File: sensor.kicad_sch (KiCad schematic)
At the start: 36 parts, among them J10 Conn_01x01_Pin, J5 Conn_01x07_Pin, J8 Conn_01x08_Pin, U3 MIC5504-3.3YM5

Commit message: Cleanup
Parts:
- removed R16: 0k, Resistor_SMD:R_0402_1005Metric_Pad0.72x0.64mm_HandSolder, symbol Device:R_Small
- JP1: footprint Jumper:SolderJumper-3_P1.3mm_Open_RoundedPad1.0x1.5mm -> Jumper:SolderJumper-3_P1.3mm_Bridged2Bar12_RoundedPad1.0x1.5mm
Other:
- note added: "By default VCC is supplied by the 5V line on the VIK connector but we can connect the 3.3V VIK source to VCC using the solder jumper, or connect the controllers 5V supply via the VCC header by cutting the jumper trace and leaving the jumber unconnected."
- note removed: "By default VCC is supplied by the 5V line on the VIK connector via the 0k resistor. If removed we can try and be compatible with the Cirque. In this case we can either connect the 3.3V VIK source to VCC using the solder jumper, or connect the controllers 5V supply via the VCC header."
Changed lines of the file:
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@@
   (junction (at 104.14 43.18) (diameter 0) (color 0 0 0 0)
-  )
-  (junction (at 176.53 33.02) (diameter 0) (color 0 0 0 0)
   )
   (junction (at 186.69 33.02) (diameter 0) (color 0 0 0 0)
@@
     (stroke (width 0) (type default))
   )
-  (wire (pts (xy 176.53 25.4) (xy 176.53 26.67))
-    (stroke (width 0) (type default))
-  )
   (wire (pts (xy 99.06 60.96) (xy 99.06 59.69))
     (stroke (width 0) (type default))
@@
     (stroke (width 0) (type default))
   )
-  (wire (pts (xy 168.91 33.02) (xy 176.53 33.02))
+  (wire (pts (xy 168.91 33.02) (xy 179.07 33.02))
     (stroke (width 0) (type default))
   )
@@
     (stroke (width 0) (type default))
   )
-  (wire (pts (xy 176.53 31.75) (xy 176.53 33.02))
-    (stroke (width 0) (type default))
-  )
   (wire (pts (xy 175.26 86.36) (xy 177.8 86.36))
     (stroke (width 0) (type default))
@@
     (stroke (width 0) (type default))
   )
-  (wire (pts (xy 176.53 33.02) (xy 179.07 33.02))
-    (stroke (width 0) (type default))
-  )
   (wire (pts (xy 121.92 87.63) (xy 127 87.63))
     (stroke (width 0) (type default))
@@
     (effects (font (size 1.27 1.27)) (justify left bottom))
   )
-  (text "By default VCC is supplied by the 5V\nline on the VIK connector via the 0k\nresistor. If removed we can try and\nbe compatible with the Cirque. In\nthis case we can either connect the\n3.3V VIK source to VCC using the solder\njumper, or connect the controllers 5V\nsupply via the VCC header."
+  (text "By default VCC is supplied by the 5V\nline on the VIK connector but we can\nconnect the 3.3V VIK source to VCC using\nthe solder jumper, or connect the\ncontrollers 5V supply via the VCC header\nby cutting the jumper trace and leaving\nthe jumber unconnected."
     (at 148.59 60.96 0)
     (effects (font (size 1.27 1.27)) (justify left bottom))
@@
   (label "CHANGE" (at 196.85 125.73 0) (fields_autoplaced)
     (effects (font (size 1.27 1.27)) (justify left bottom))
-  )
-  (label "VIK_5V" (at 176.53 25.4 180) (fields_autoplaced)
-    (effects (font (size 1.27 1.27)) (justify right bottom))
   )
   (label "SCL" (at 72.39 119.38 180) (fields_autoplaced)
@@
       (effects (font (size 1.27 1.27)) hide)
     )
-    (property "Footprint" "Jumper:SolderJumper-3_P1.3mm_Open_RoundedPad1.0x1.5mm" (at 160.02 29.21 0)
+    (property "Footprint" "Jumper:SolderJumper-3_P1.3mm_Bridged2Bar12_RoundedPad1.0x1.5mm" (at 160.02 29.21 0)
       (effects (font (size 1.27 1.27)) hide)
     )
@@
         )
       )
-    )
-  )
-  (symbol (lib_id "Device:R_Small") (at 176.53 29.21 0) (unit 1)
-    (in_bom yes) (on_board yes) (dnp no) (fields_autoplaced)
-    (property "Reference" "R16" (at 179.07 27.94 0)
-      (effects (font (size 1.27 1.27)) (justify left))
-    )
-    (property "Value" "0k" (at 179.07 30.48 0)
-      (effects (font (size 1.27 1.27)) (justify left))
-    )
-    (property "Footprint" "Resistor_SMD:R_0402_1005Metric_Pad0.72x0.64mm_HandSolder" (at 176.53 29.21 0)
-      (effects (font (size 1.27 1.27)) hide)
-    )
-    (property "Datasheet" "~" (at 176.53 29.21 0)
-      (effects (font (size 1.27 1.27)) hide)
-    )
-    (property "LCSC" "C17168" (at 179.07 27.94 0)
-      (effects (font (size 1.27 1.27)) hide)
-    )
-    (pin "2")
-    (pin "1")
-    (instances
-      (project "trackpad"
-        (path "/3796446b-0052-4d89-b512-07a2e9135d0d/2780c9a8-e5e0-42e8-93d7-9eb6f8aa439b"
-          (reference "R16") (unit 1)
-        )
-      )

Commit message: Modifications before initial order.
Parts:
- C29: LCSC C52923 -> C1525
- R10: LCSC C25744 -> C25752
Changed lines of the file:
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@@
       (effects (font (size 1.27 1.27)) hide)
     )
-    (property "LCSC" "C25744" (at 176.53 36.83 0)
+    (property "LCSC" "C25752" (at 176.53 36.83 0)
       (effects (font (size 1.27 1.27)) hide)
     )
@@
       (effects (font (size 1.27 1.27)) hide)
     )
-    (property "LCSC" "C52923" (at 226.06 34.2963 0)
+    (property "LCSC" "C1525" (at 226.06 34.2963 0)
       (effects (font (size 1.27 1.27)) hide)
     )
@@
       (effects (font (size 1.27 1.27)) hide)
     )
-    (property "LCSC" "C52923" (at 180.34 35.56 0)
-      (effects (font (size 1.27 1.27)) hide)
-    )
+    (property "LCSC" "C1525" (at 180.34 35.56 0)
+      (effects (font (size 1.27 1.27)) hide)
+    )

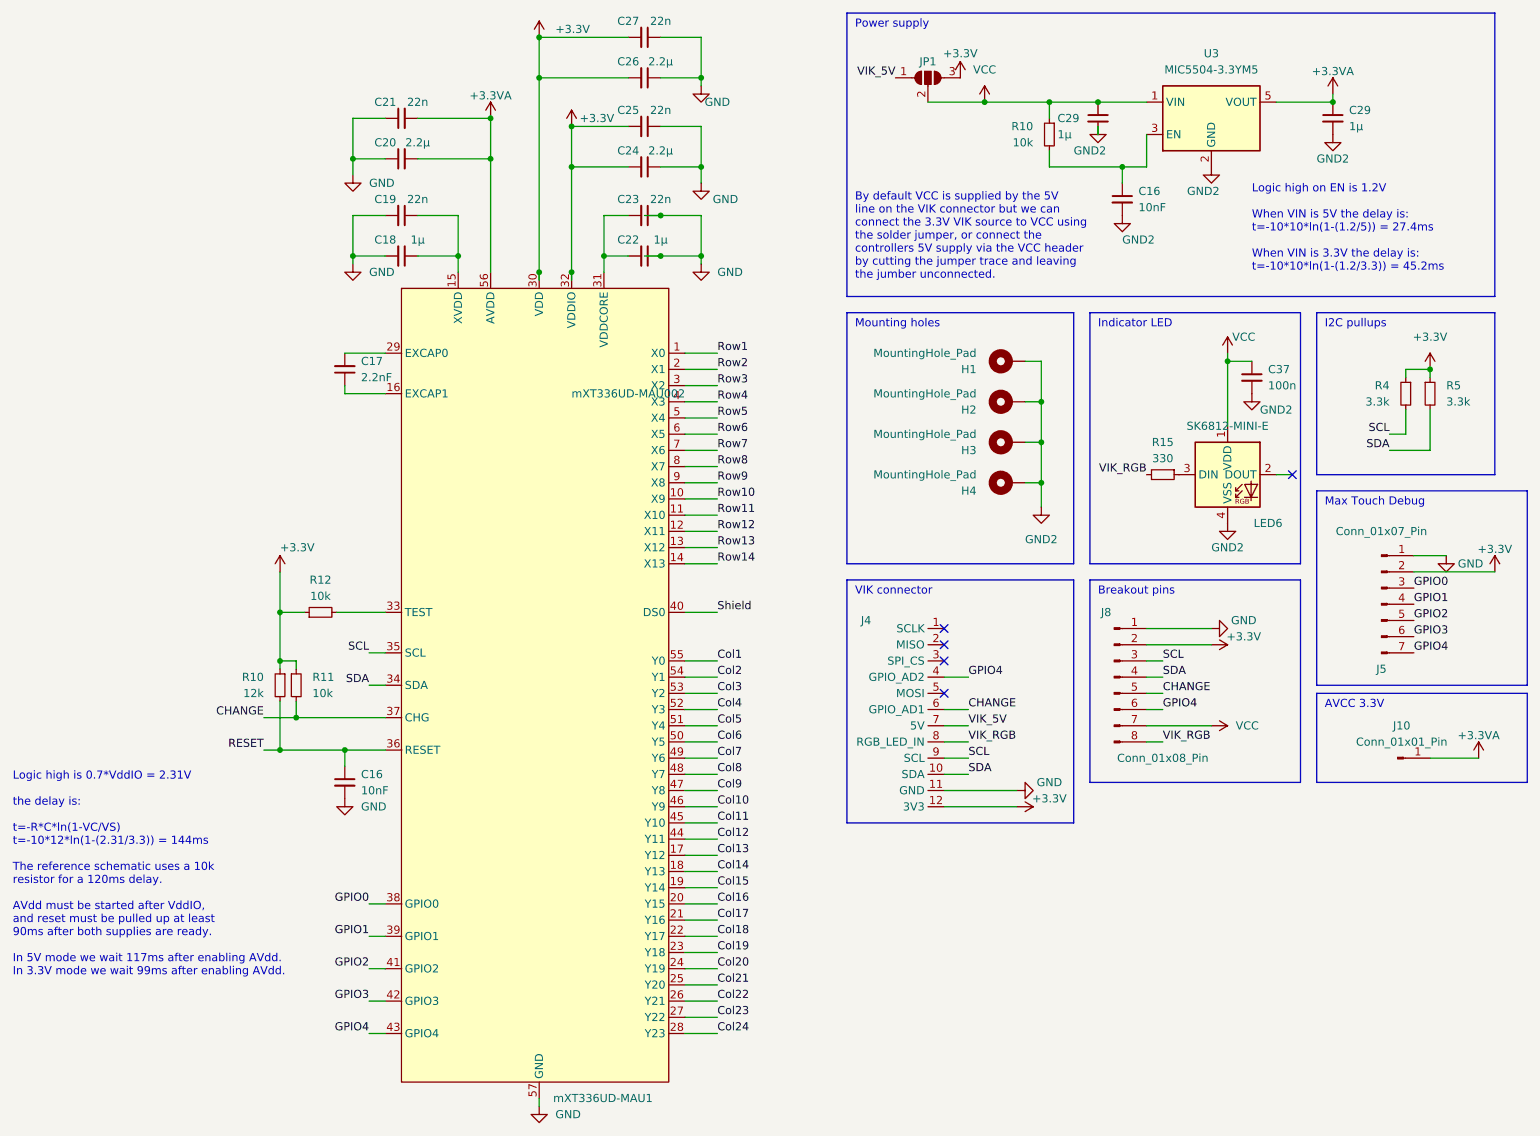
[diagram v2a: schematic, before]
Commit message: Fixes for minor issues in the v1.0 PCB.
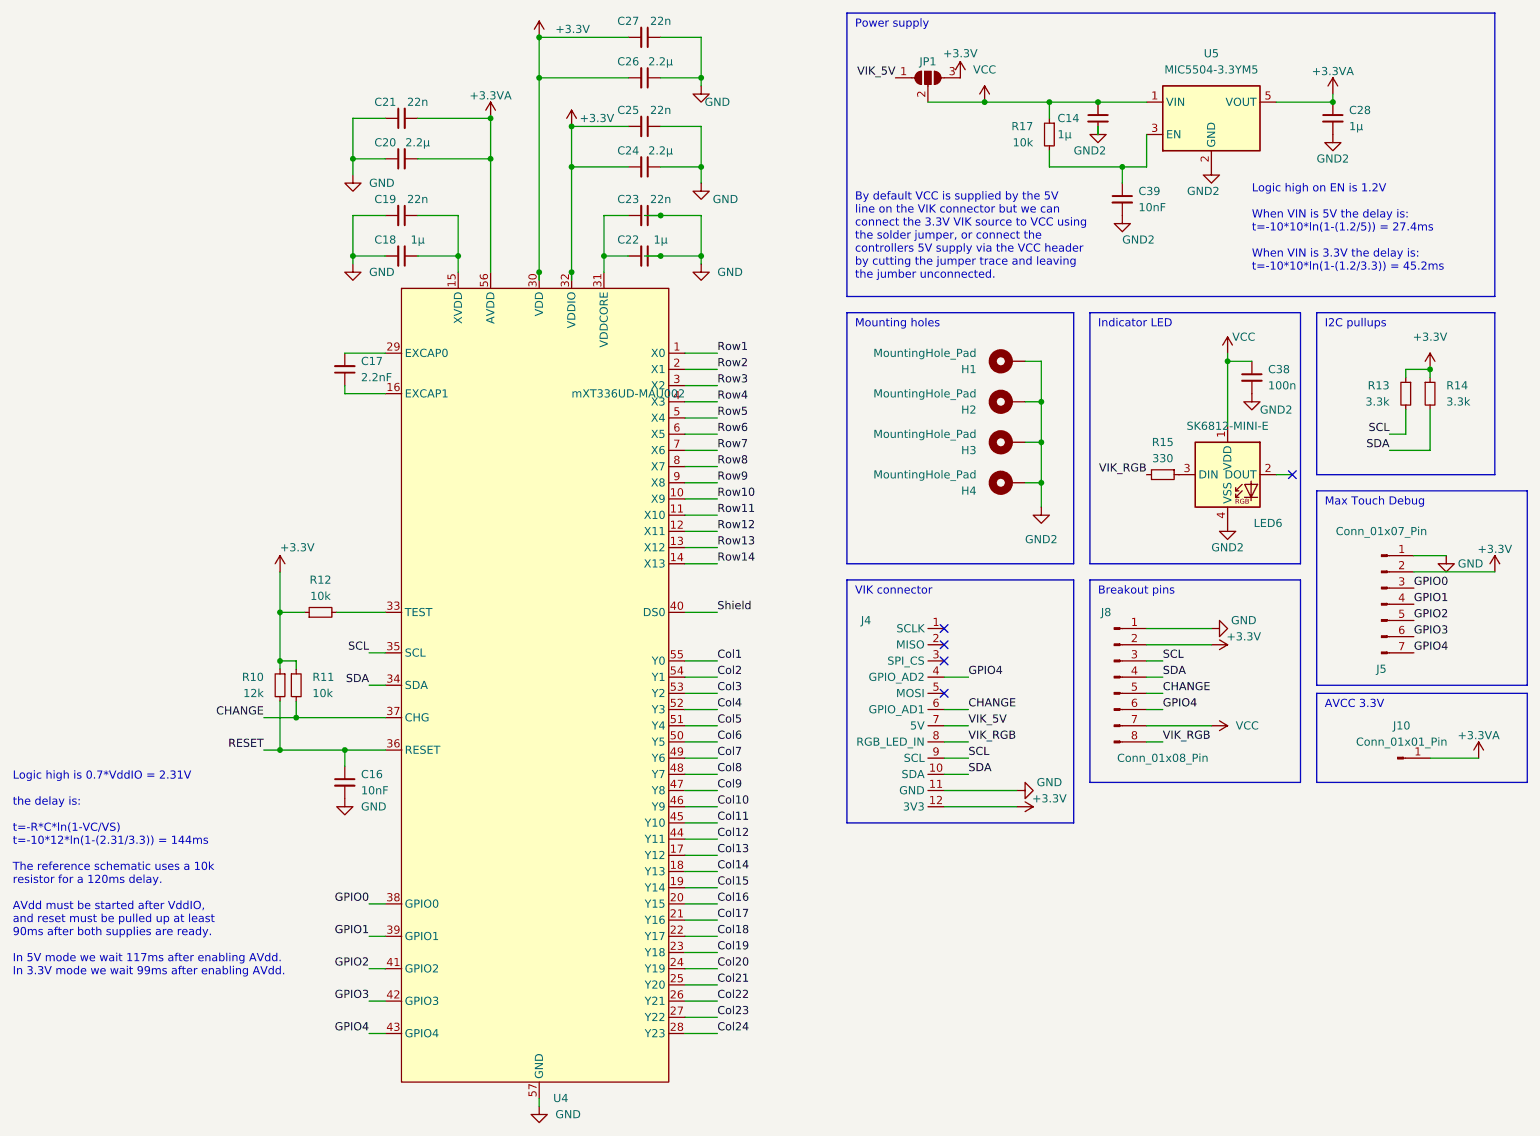
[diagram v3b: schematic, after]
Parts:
- renumbered C29 to C14, C29 to C28, C37 to C38, C16 to C39, R4 to R13, R5 to R14, R10 to R17, mXT336UD-MAU1 to U4, U3 to U5

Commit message: Fixup LSCS part number miss-match between PCB and schematic.
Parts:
- C14, C28: LCSC C1525 -> C52923
- R17: LCSC C25752 -> C25744
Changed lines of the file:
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@@
       (effects (font (size 1.27 1.27)) hide)
     )
-    (property "LCSC" "C25752" (at 176.53 36.83 0)
+    (property "LCSC" "C25744" (at 176.53 36.83 0)
       (effects (font (size 1.27 1.27)) hide)
     )
@@
       (effects (font (size 1.27 1.27)) hide)
     )
-    (property "LCSC" "C1525" (at 226.06 34.2963 0)
+    (property "LCSC" "C52923" (at 226.06 34.2963 0)
       (effects (font (size 1.27 1.27)) hide)
     )
@@
       (effects (font (size 1.27 1.27)) hide)
     )
-    (property "LCSC" "C1525" (at 180.34 35.56 0)
-      (effects (font (size 1.27 1.27)) hide)
-    )
+    (property "LCSC" "C52923" (at 180.34 35.56 0)
+      (effects (font (size 1.27 1.27)) hide)
+    )

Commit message: Fix minor issues reported by JLC, and replace parts which are often out of stock.
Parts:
- H1, H2, H3, H4, J10, J5, J8, JP1: now left out of the parts list
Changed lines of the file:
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@@
   )
   (symbol (lib_id "Mechanical:MountingHole_Pad") (at 172.72 86.36 90) (unit 1)
-    (in_bom yes) (on_board yes) (dnp no)
+    (in_bom no) (on_board yes) (dnp no)
     (property "Reference" "H3" (at 167.64 87.63 90)
       (effects (font (size 1.27 1.27)) (justify left))
@@
   )
   (symbol (lib_id "Connector:Conn_01x07_Pin") (at 231.14 111.76 0) (unit 1)
-    (in_bom yes) (on_board yes) (dnp no)
+    (in_bom no) (on_board yes) (dnp no)
     (property "Reference" "J5" (at 231.14 121.92 0)
       (effects (font (size 1.27 1.27)))
@@
   )
   (symbol (lib_id "Connector:Conn_01x01_Pin") (at 233.68 135.89 0) (unit 1)
-    (in_bom yes) (on_board yes) (dnp no) (fields_autoplaced)
+    (in_bom no) (on_board yes) (dnp no) (fields_autoplaced)
     (property "Reference" "J10" (at 234.315 130.81 0)
       (effects (font (size 1.27 1.27)))
@@
   )
   (symbol (lib_id "Mechanical:MountingHole_Pad") (at 172.72 73.66 90) (unit 1)
-    (in_bom yes) (on_board yes) (dnp no)
+    (in_bom no) (on_board yes) (dnp no)
     (property "Reference" "H1" (at 167.64 74.93 90)
       (effects (font (size 1.27 1.27)) (justify left))
@@
   )
   (symbol (lib_id "Mechanical:MountingHole_Pad") (at 172.72 80.01 90) (unit 1)
-    (in_bom yes) (on_board yes) (dnp no)
+    (in_bom no) (on_board yes) (dnp no)
     (property "Reference" "H2" (at 167.64 81.28 90)
       (effects (font (size 1.27 1.27)) (justify left))
@@
   )
   (symbol (lib_id "Connector:Conn_01x08_Pin") (at 189.23 123.19 0) (unit 1)
-    (in_bom yes) (on_board yes) (dnp no)
+    (in_bom no) (on_board yes) (dnp no)
     (property "Reference" "J8" (at 187.96 113.03 0)
       (effects (font (size 1.27 1.27)))
@@
   )
   (symbol (lib_id "Jumper:SolderJumper_3_Open") (at 160.02 29.21 0) (unit 1)
-    (in_bom yes) (on_board yes) (dnp no)
+    (in_bom no) (on_board yes) (dnp no)
     (property "Reference" "JP1" (at 160.02 26.67 0)
       (effects (font (size 1.27 1.27)))
@@
   )
   (symbol (lib_id "Mechanical:MountingHole_Pad") (at 172.72 92.71 90) (unit 1)
-    (in_bom yes) (on_board yes) (dnp no)
+    (in_bom no) (on_board yes) (dnp no)
     (property "Reference" "H4" (at 167.64 93.98 90)
       (effects (font (size 1.27 1.27)) (justify left))
